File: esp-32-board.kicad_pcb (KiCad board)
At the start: 2 copper layers, 53.8 x 69.1 mm, 32 parts, among them J1 Conn_Arduino_UNO_R3, J2 Conn_02x03_Odd_Even, J3 ESP-PROG-Program, J4 ESP-PROG-Debug, J5 Barrel_Jack_MountingPin, J6 USB_B_Micro, Q1 BCR129S, SW1 SW_Push, SW2 SW_Push, SW3 SW_SPST, U1 ESP32-WROOM-32, U3 NCP1117-3.3, U4 NCP1117ST50T3G, U5 USBLC6-2SC6, U6 CP2102N-A01-GQFN28

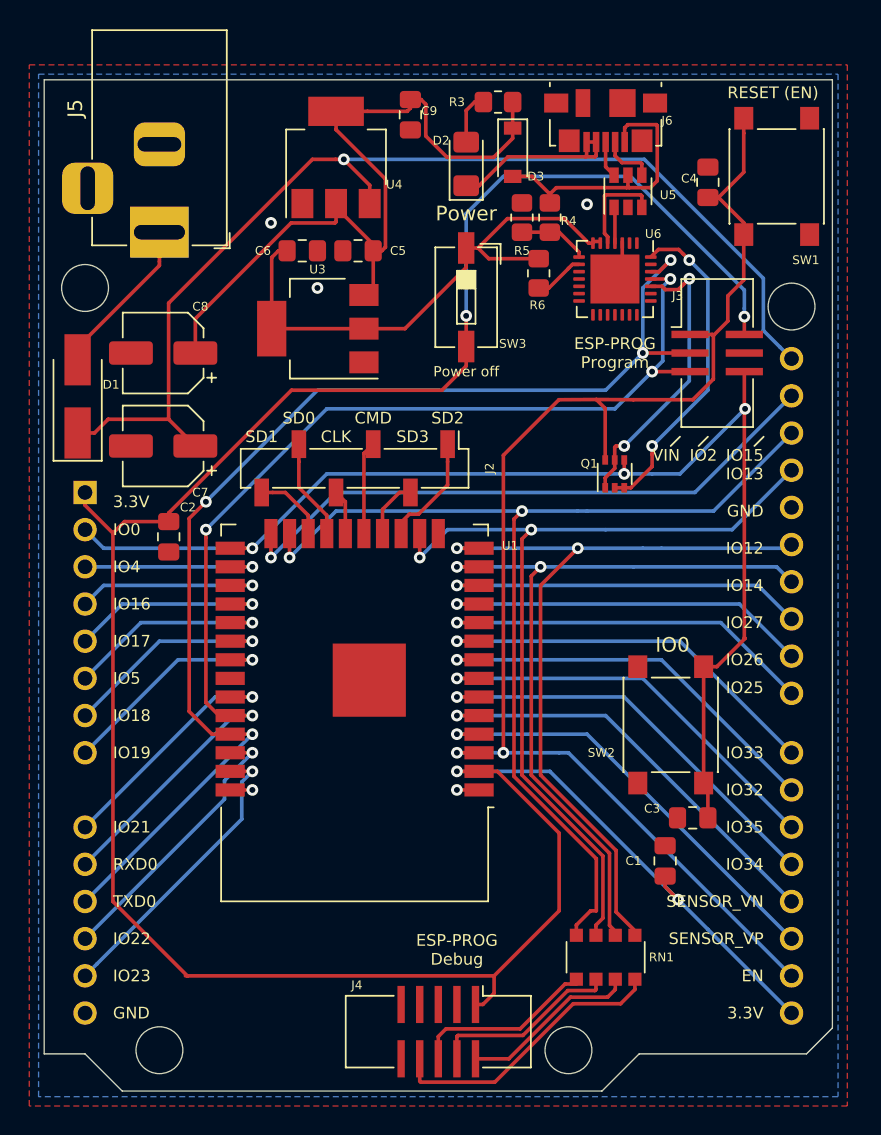
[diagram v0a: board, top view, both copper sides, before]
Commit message: Update power switch
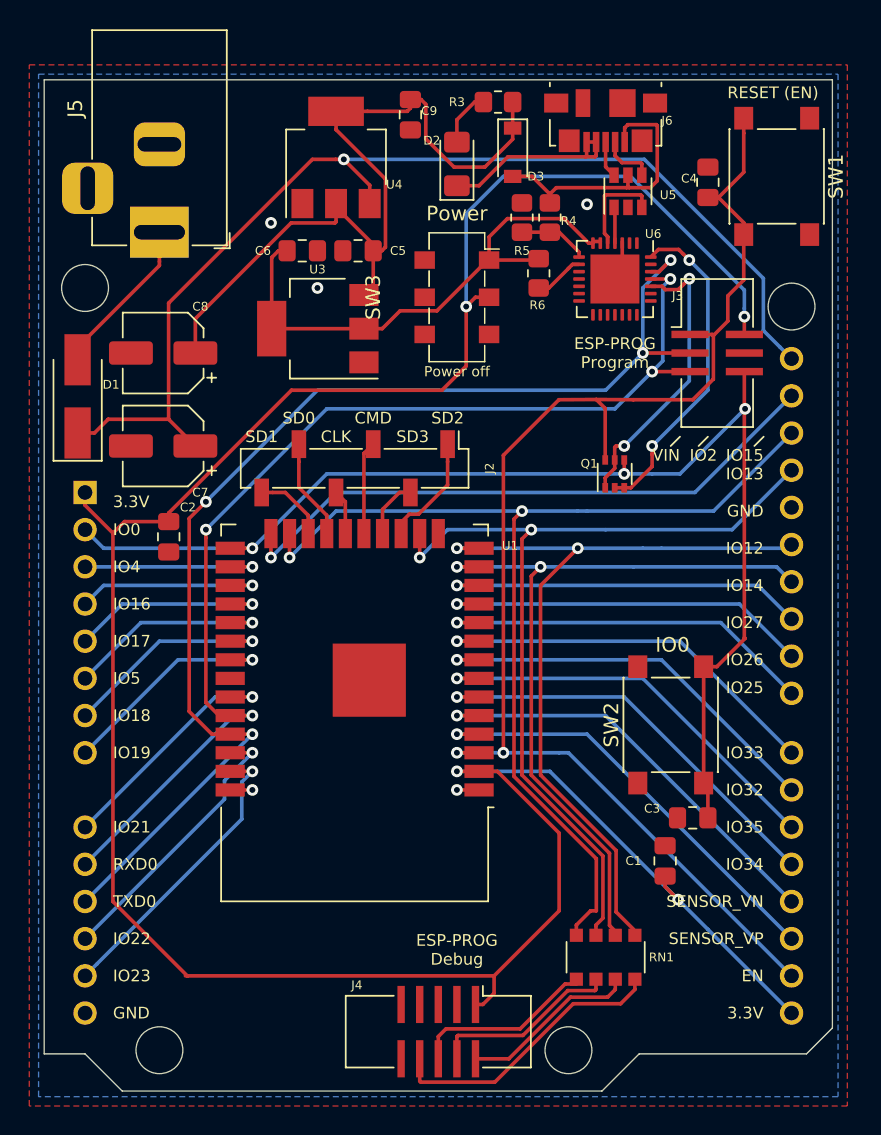
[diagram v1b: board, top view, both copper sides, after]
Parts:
- SW1, SW2: footprint Button_Switch_SMD:SW_Push_1P1T_NO_6x6mm_H9.5mm -> Button_Switch_SMD:SW_Push_1P1T_NO_6x6mm_H4.3mm
- SW3: value SW_SPST -> SW_DPDT_x2; footprint Button_Switch_SMD:SW_DIP_SPSTx01_Slide_6.7x4.1mm_W6.73mm_P2.54mm_LowProfile_JPin -> Button_Switch_SMD:Nidec_CL-SB-22B-0X
- moved D2 0.64 mm to (157.5, 27.1)
- moved SW3 0.64 mm to (157.5, 36.2)
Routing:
- net +3V3: track 177.7 -> 179.5 mm
- net /Power/Internal_3V3: track 37.6 -> 36.7 mm
- net +5V: track 53.8 -> 54.5 mm
- net GND: track 18.2 -> 18.9 mm

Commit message: Update layout
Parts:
- moved C3 24.0 mm to (168.5, 48.3)
- moved SW2 10.7 mm to (171.1, 54.8)
- moved Q1 8.53 mm to (166.1, 40.0), turned to 180 degrees
- moved C4 3.75 mm to (175.0, 24.6), turned to 90 degrees
- moved SW1 0.51 mm to (179.3, 27.4)
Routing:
- net /USB/DTR: track 22.5 -> 13.0 mm, vias 2 -> 0
- net /USB/RTS: track 20.0 -> 11.3 mm, vias 2 -> 0
- net /IO0: track 84.3 -> 87.7 mm
- net /EN: track 94.3 -> 93.5 mm

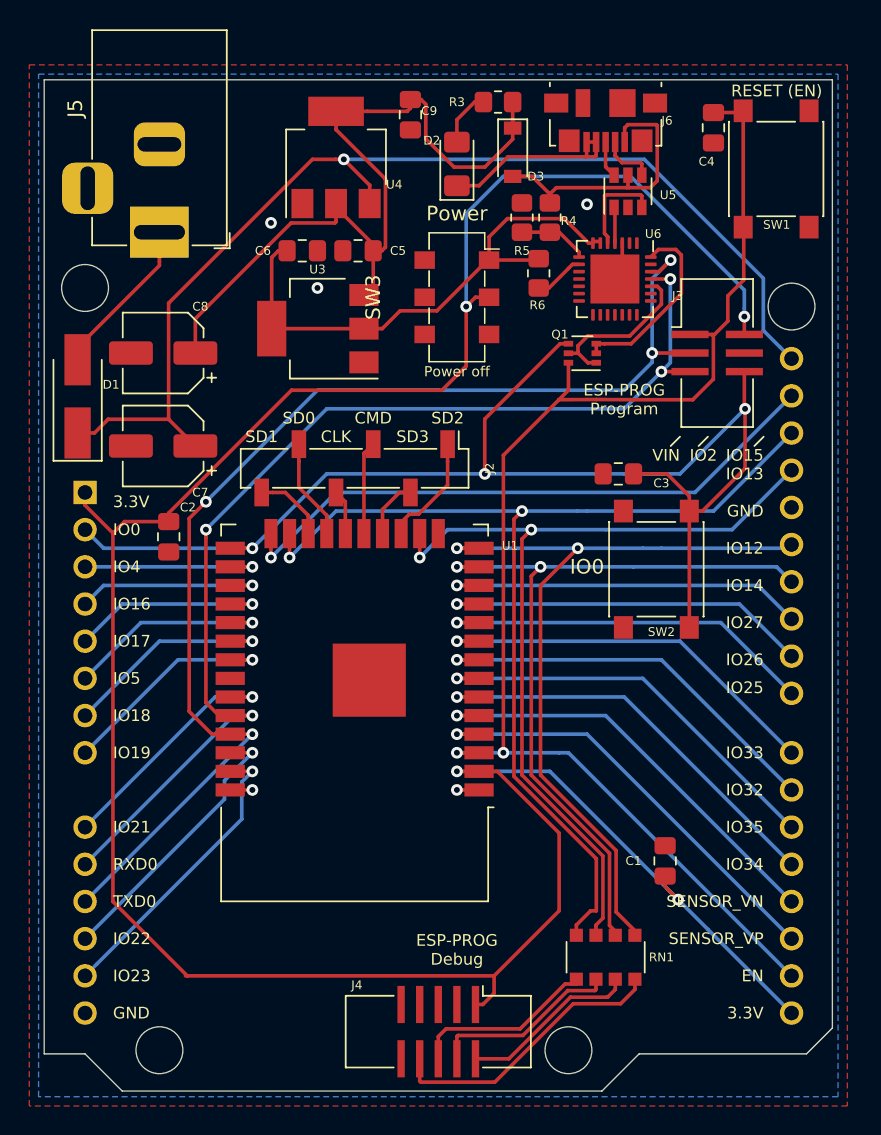
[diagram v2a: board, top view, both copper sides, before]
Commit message: Schematic reorganization & reannotate
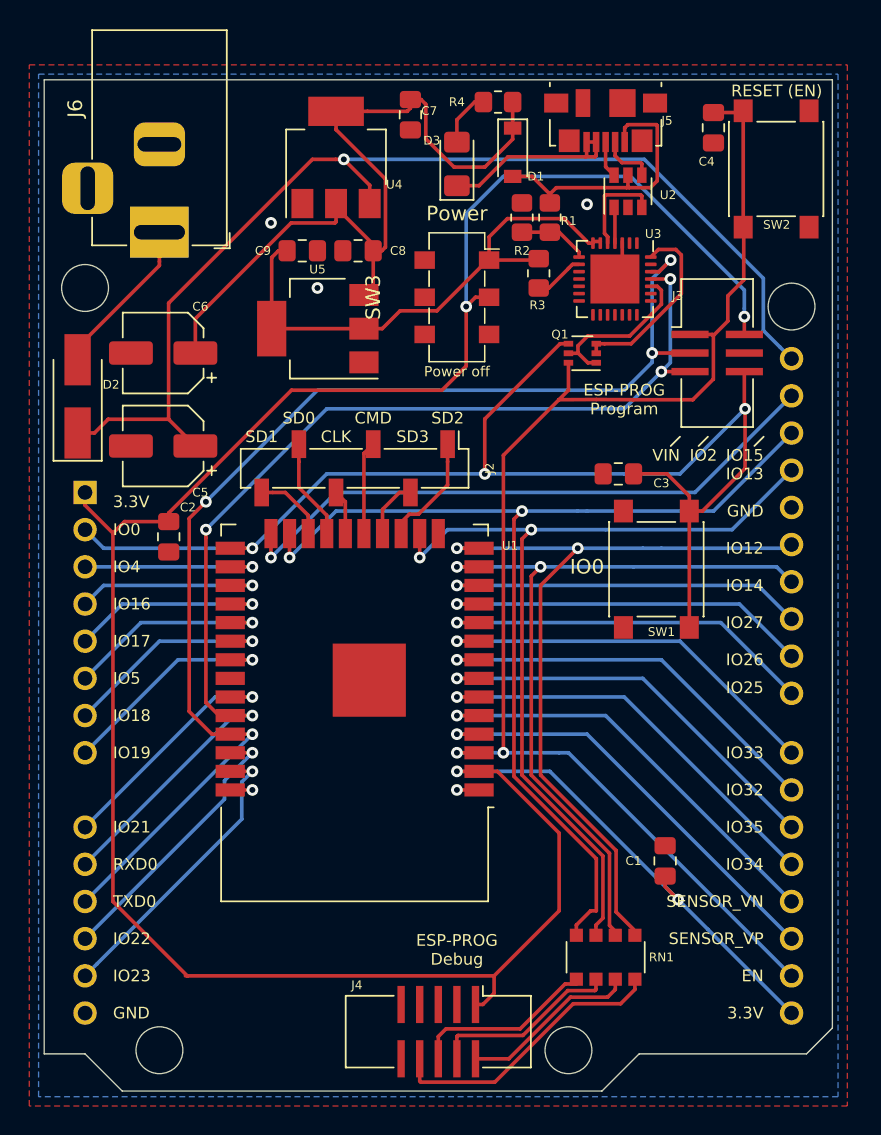
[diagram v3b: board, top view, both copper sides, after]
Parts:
- renumbered C7 to C5, C8 to C6, C9 to C7, C5 to C8, C6 to C9, D3 to D1, D1 to D2, D2 to D3, J6 to J5, J5 to J6, R4 to R1, R5 to R2, R6 to R3, R3 to R4, SW2 to SW1, SW1 to SW2, U5 to U2, U6 to U3, U3 to U5

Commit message: feat: optimize layout
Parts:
- moved C1 11.2 mm to (172.3, 85.9), turned to 180 degrees
- moved RN1 1.37 mm to (169.0, 81.3)
- moved C3 1.27 mm to (169.8, 48.3)
- moved R3 0.94 mm to (162.8, 33.7), turned to 180 degrees
- moved C2 0.76 mm to (137.8, 51.8)
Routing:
- net +3V3: track 179.5 -> 158.2 mm, vias 4 -> 6
- net /EN: track 93.5 -> 88.4 mm
- net Net-(J4-Pad8): track 19.6 -> 21.5 mm
- net /TXD0: track 82.1 -> 84.0 mm
- net /IO12: track 54.6 -> 53.1 mm
- net /RXD0: track 76.4 -> 77.9 mm
- net /IO22: track 18.9 -> 20.4 mm
- net /IO21: track 16.6 -> 18.1 mm
- net Net-(J4-Pad4): track 13.1 -> 14.4 mm
- net Net-(J4-Pad2): track 12.2 -> 13.6 mm
- net VDC: track 75.2 -> 76.6 mm
- net Net-(R3-Pad1): track 3.43 -> 2.12 mm
- net /IO0: track 87.7 -> 86.5 mm
- net /IO15: track 71.8 -> 70.5 mm
- net Net-(J4-Pad6): track 12.8 -> 13.9 mm
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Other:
- outline, holes or cut-outs redrawn
- net class Power added: clearance 0.2, trace_width 0.25, via_dia 0.8, via_drill 0.4
